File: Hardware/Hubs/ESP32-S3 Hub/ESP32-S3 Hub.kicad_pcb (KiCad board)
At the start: 6 copper layers, 15 x 30 mm, 56 parts, among them J1 Precidip 853-87-004-20-001101, J10 Precidip 853-87-004-20-001101, J11 7 pin FPC 0.3mm Aces 51688-00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, J12 Precidip 853-87-004-20-001101, J13 TE 3-2363961-0 receptacle, J15 Precidip 853-87-004-20-001101, J16 TE 3-2363961-0 receptacle, J18 Precidip 852-10-004-20-001101, J2 Precidip 853-87-004-20-001101, J3 7 pin FPC 0.3mm Aces 51688-00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, J4 Precidip 853-87-004-20-001101, J5 7 pin FPC 0.3mm Aces 51688-00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, J6 Precidip 853-87-004-20-001101, J7 Precidip 853-87-004-20-001101, J8 7 pin FPC 0.3mm Aces 51688-00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, J9 Precidip 853-87-004-20-001101, SW1 Mitsumi R-667996, SW2 Mitsumi R-667996, U1 ESP32-S3, U2 IS31FL3726A-QFLS4, U3 THVD1420DRLR, Y1 ABM11-40.000MHZ-B1U-T3, 10ppm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

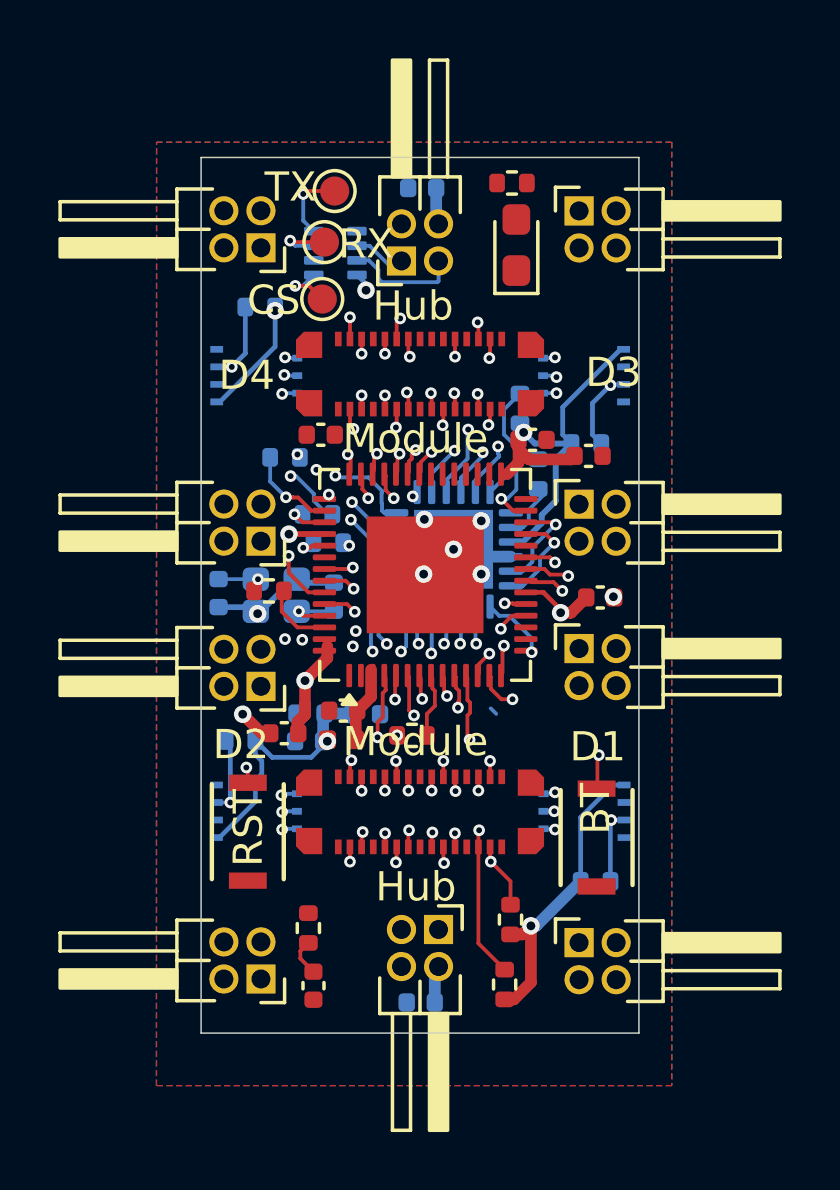
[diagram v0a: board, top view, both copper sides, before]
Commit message: Swapped around pins and routed main driver outputs
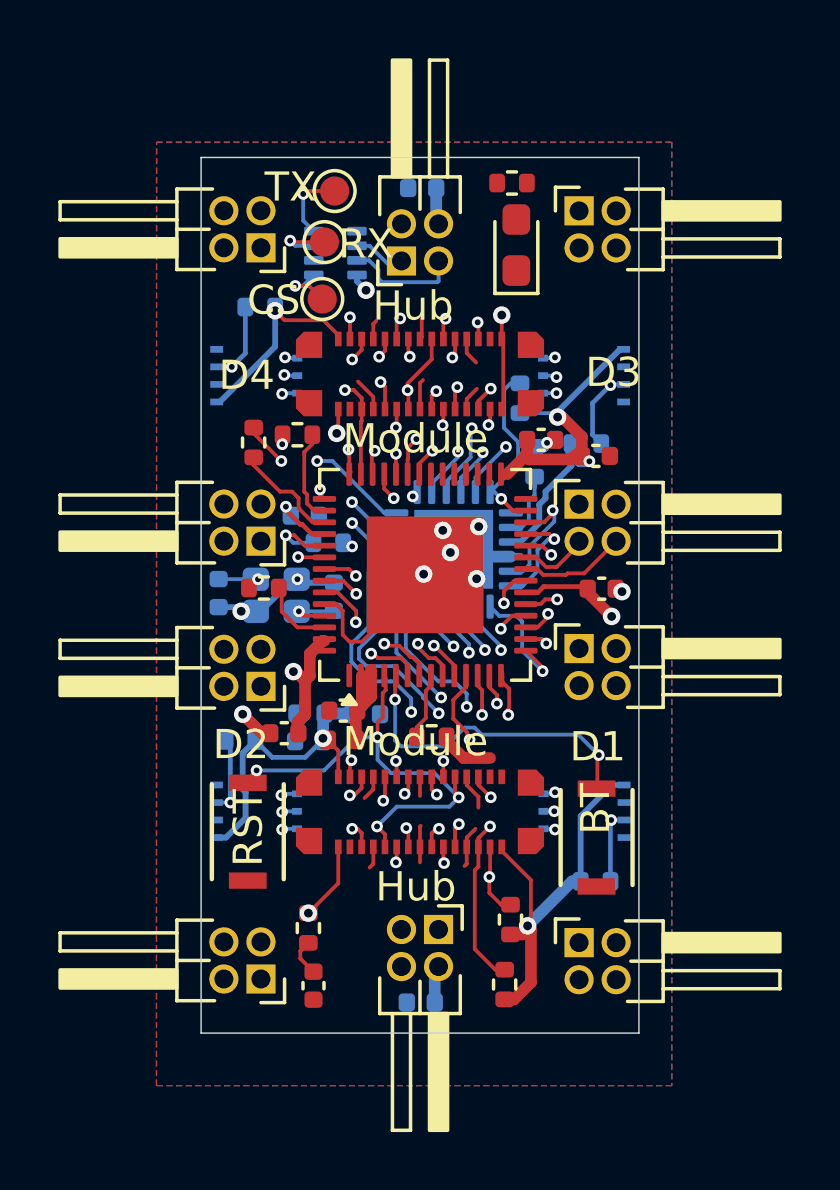
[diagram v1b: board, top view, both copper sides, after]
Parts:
- C10: moved to B.Cu
- R3, R4: moved to F.Cu
- moved R4 3.29 mm to (149.7, 91.6), turned to 90 degrees
- moved C10 2.83 mm to (151.5, 94.1), turned to 0 degrees
- moved R3 0.88 mm to (151.2, 91.3), turned to 180 degrees
- moved R1 0.68 mm to (155.8, 101.7), turned to 0 degrees
- moved R12 0.44 mm to (159.3, 92.2)
- moved R11 0.35 mm to (158.8, 90.0)
- moved C8 0.30 mm to (161.6, 96.6)
- moved C5 0.30 mm to (159.6, 91.5)
- moved C7 0.25 mm to (161.4, 92.0)
- moved R6 0.20 mm to (150.1, 96.5)
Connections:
- C8 pad 1: VDD -> unconnected-(C8-Pad1)
- C8 pad 2: GND -> unconnected-(C8-Pad2)
- J1 pad 3: unconnected-(J1-Pin_3-Pad3) -> 1CSA-C
- J1 pad 4: unconnected-(J1-Pin_4-Pad4) -> 1CSA-D
- J10 pad 3: unconnected-(J10-Pin_3-Pad3) -> 4CSA-C
- J10 pad 4: unconnected-(J10-Pin_4-Pad4) -> 4CSA-D
- J15 pad 4: unconnected-(J15-Pin_4-Pad4) -> 1D
- J2 pad 4: unconnected-(J2-Pin_4-Pad4) -> 2D
- J4 pad 3: unconnected-(J4-Pin_3-Pad3) -> 2CSA-C
- J4 pad 4: unconnected-(J4-Pin_4-Pad4) -> 2CSA-D
- J6 pad 4: unconnected-(J6-Pin_4-Pad4) -> 3D
- J7 pad 3: unconnected-(J7-Pin_3-Pad3) -> 3CSA-C
- J7 pad 4: unconnected-(J7-Pin_4-Pad4) -> 3CSA-D
- J9 pad 4: unconnected-(J9-Pin_4-Pad4) -> 4D
- U1 pad 10: 4CSA-D -> 2CSA-B
- U1 pad 11: 3CSA-B -> 1CSA-D
- U1 pad 12: 3CSA-A -> 1CSA-C
- U1 pad 13: 3CSA-C -> 1CSA-A
- U1 pad 14: 3CSA-D -> 1CSA-B
- U1 pad 16: 2CSA-A -> 4CSA-C
- U1 pad 17: 2CSA-B -> 4CSA-D
- U1 pad 18: 2CSA-C -> 4CSA-B
- U1 pad 19: 2CSA-D -> 3CSA-B
- U1 pad 21: 1CSA-C -> 4CSA-A
- U1 pad 22: 1CSA-D -> 3CSA-D
- U1 pad 23: 1CSA-A -> 3CSA-C
- U1 pad 24: 1CSA-B -> 3CSA-A
- U1 pad 6: 4CSA-A -> 2CSA-C
- U1 pad 7: 4CSA-B -> 2CSA-D
- U1 pad 9: 4CSA-C -> 2CSA-A
- U2 pad 10: 1B -> 1C
- U2 pad 12: 2A -> 2B
- U2 pad 13: 2B -> 2D
- U2 pad 14: 2C -> 2A
- U2 pad 15: 2D -> 2C
- U2 pad 16: 3A -> 4B
- U2 pad 17: 3B -> 4A
- U2 pad 18: 3C -> 4D
- U2 pad 19: 3D -> 4C
- U2 pad 20: 4A -> 3A
- U2 pad 21: 4B -> 3B
- U2 pad 22: 4C -> 3D
- U2 pad 23: 4D -> 3C
- U2 pad 8: 1C -> 1B
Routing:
- net UART0_TX: track 5.26 -> 36.1 mm, vias 5 -> 6
- net RS485-: track 1.98 -> 31.8 mm
- net UART0_RX: track 4.66 -> 33.1 mm
- net RS485+: track 3.99 -> 31.4 mm
- net NRST: track 6.02 -> 32.6 mm
- net 4CSA-D: track 1.19 -> 21.8 mm
- net 4CSA-C: track 0.67 -> 20.7 mm
- net 2A: track 1.29 -> 21.2 mm
- net 4CSA-B: track 0.75 -> 20.0 mm
- net 2B: track 2.46 -> 21.6 mm
- net GND: track 9.60 -> 28.3 mm, vias 14 -> 9
- net VDD: track 50.2 -> 68.6 mm, vias 8 -> 12
- net 2C: track 3.10 -> 19.4 mm
- net 4CSA-A: track 1.46 -> 17.7 mm
- net 2D: track 3.80 -> 18.8 mm
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
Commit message: Finished routing with current components
I may add some protection and isolation stuff
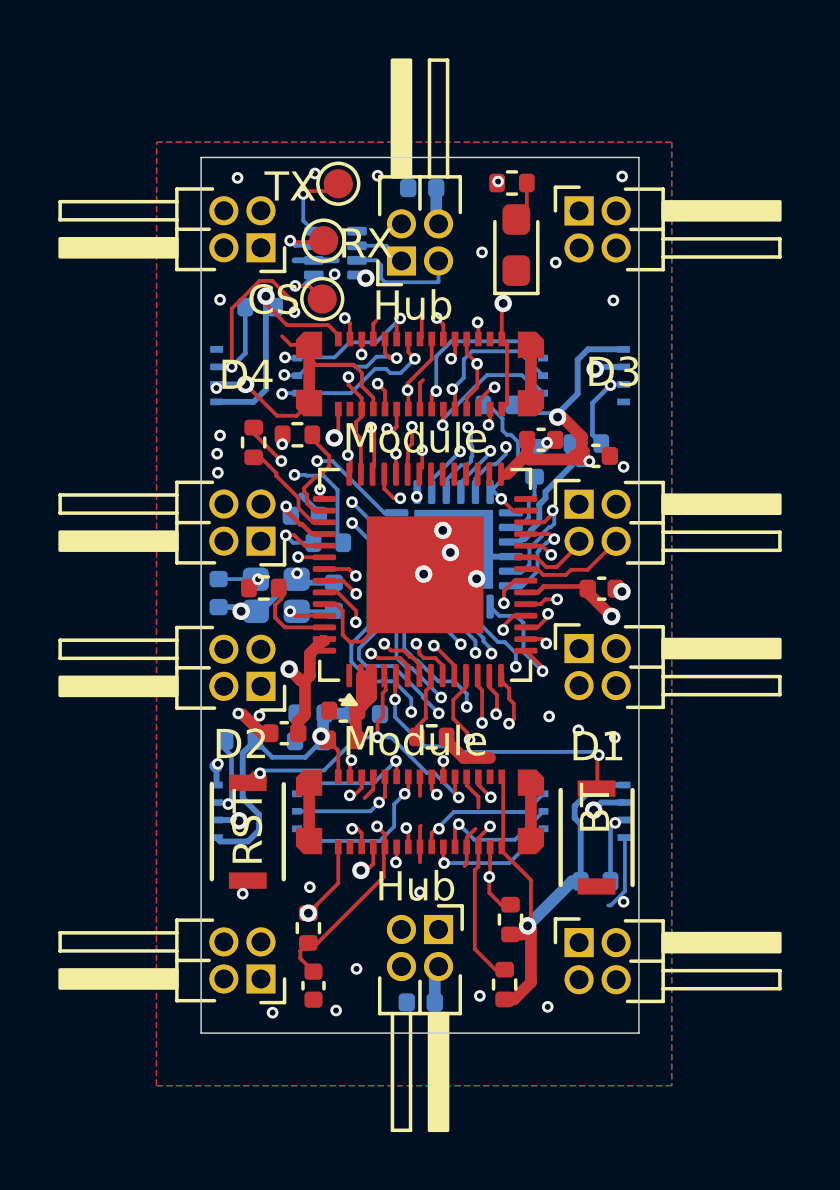
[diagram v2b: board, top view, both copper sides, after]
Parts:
- moved R11 0.78 mm to (158.1, 90.3), turned to 0 degrees
- moved TP3 0.28 mm to (152.6, 82.7)
- moved TP20 0.06 mm to (152.1, 84.7)
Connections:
- C8 pad 1: unconnected-(C8-Pad1) -> VDD
- C8 pad 2: unconnected-(C8-Pad2) -> GND
- U1 pad 36: CS4 -> CS1
- U1 pad 38: CS2 -> CS4
- U1 pad 39: CS1 -> CS2
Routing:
- net MISO1: track 5.33 -> 51.5 mm, vias 9 -> 6
- net MOSI1: track 9.89 -> 48.2 mm, vias 9 -> 6
- net SCK1: track 6.50 -> 42.6 mm, vias 9 -> 6
- net GND: track 28.3 -> 55.1 mm, vias 9 -> 42
- net SDA1: track 16.5 -> 42.4 mm
- net LED: track 1.75 -> 26.9 mm, vias 1 -> 2
- net CS2: track 3.24 -> 28.1 mm
- net CS3: track 4.05 -> 26.8 mm, vias 2 -> 3
- net CS1: track 3.51 -> 23.3 mm
- net SCL1: track 19.9 -> 39.2 mm
- net Free1: track 6.63 -> 24.8 mm
- net CS4: track 3.62 -> 15.4 mm, vias 2 -> 3
- net VDD: track 68.6 -> 80.2 mm
- net Free2: track 3.88 -> 12.3 mm
- net UART0_TX: track 36.1 -> 43.9 mm
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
